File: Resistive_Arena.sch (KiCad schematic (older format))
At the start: 15 parts, among them P1 1360_2_PIN, P2 1360_2_PIN, P3 1360_2_PIN, P4 1360_2_PIN, P5 1360_2_PIN, P6 1360_2_PIN, P7 1360_2_PIN, P8 1360_2_PIN

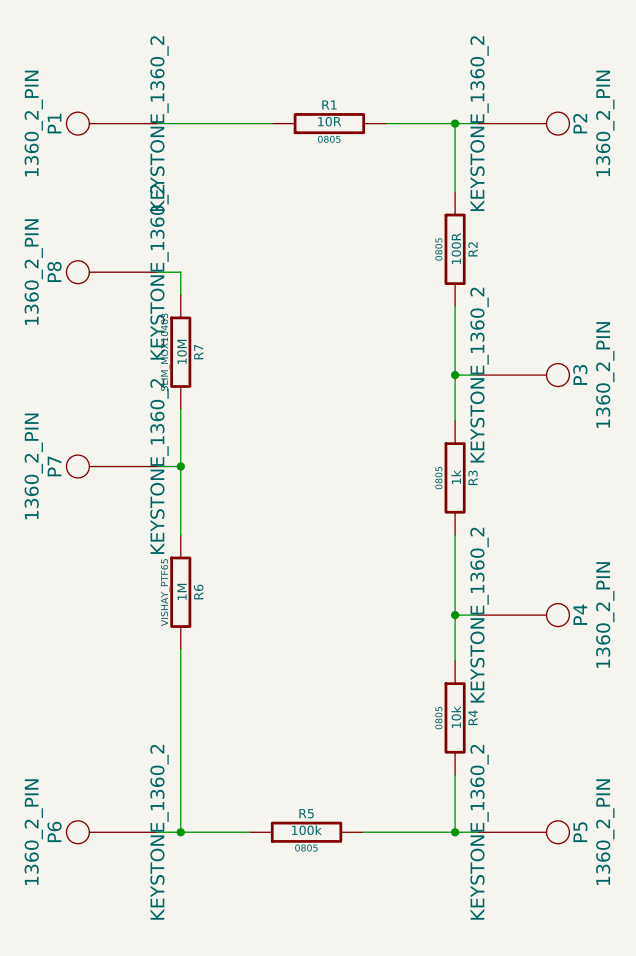
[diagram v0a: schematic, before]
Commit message: Added models for 3D pcb view
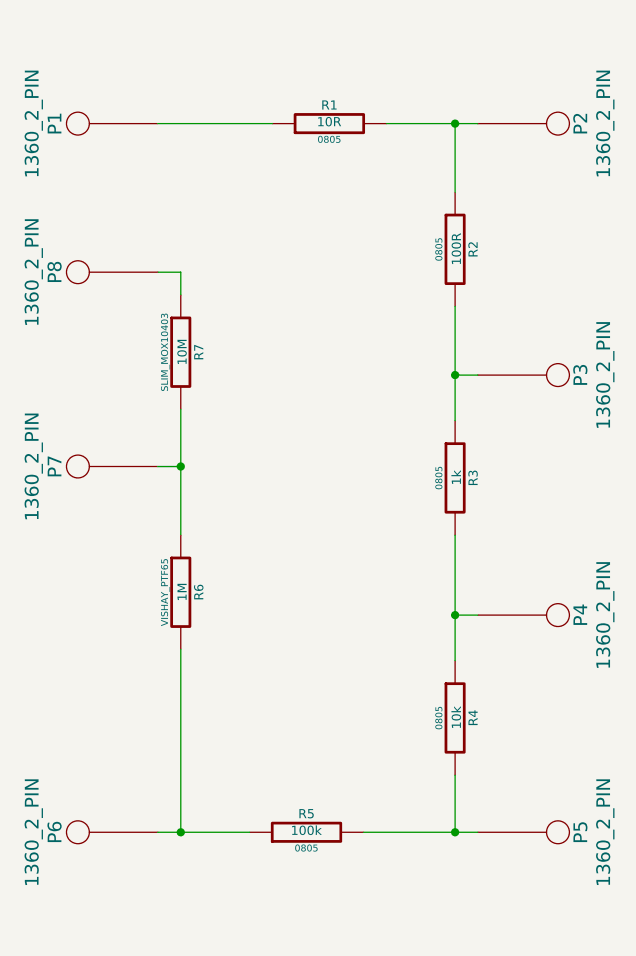
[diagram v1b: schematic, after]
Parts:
- P1, P2, P3, P4, P5, P6, P7, P8: Manufacturer (none) -> Keystone; Part Number (none) -> 1360-2; Source (none) -> Mouser
- R1: Manufacturer (none) -> TE Connectivity; Part Number (none) -> RN73C2A10RBTG; Source (none) -> Mouser
- R2: Manufacturer (none) -> Welwyn-TT; Part Number (none) -> PCF0805-13-100RBT1; Source (none) -> Mouser
- R3: Manufacturer (none) -> Welwyn-TT; Part Number (none) -> PCF0805-13-1K0BT1; Source (none) -> Mouser
- R4: Manufacturer (none) -> Welwyn-TT; Part Number (none) -> PCF0805-13-10KBT1; Source (none) -> Mouser
- R5: Manufacturer (none) -> Vishay; Part Number (none) -> TNPU0805100KAZEN00; Source (none) -> Mouser
- R6: Manufacturer (none) -> Vishay; Part Number (none) -> PTF651M0000BZBF; Source (none) -> Mouser
- R7: Manufacturer (none) -> Ohmite; Part Number (none) -> SM104031005FE; Source (none) -> Mouser
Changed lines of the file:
@@
 F 1 "10R" V 5157 1701 40  0000 C CNN
 F 2 "0805" V 5080 1700 30  0000 C CNN
-F 3 "" H 5150 1700 30  0000 C CNN
+F 3 "http://documents.tycoelectronics.com/commerce/DocumentDelivery/DDEController?Action=showdoc&DocId=Data+Sheet%7F1773270%7FK%7Fpdf%7FEnglish%7FENG_DS_1773270_K.pdf" H 5150 1700 30  0001 C CNN
+F 4 "TE Connectivity" V 5150 1700 60  0001 C CNN "Manufacturer"
+F 5 "RN73C2A10RBTG" V 5150 1700 60  0001 C CNN "Part Number"
+F 6 "Mouser" V 5150 1700 60  0001 C CNN "Source"
 	1    5150 1700
 	0    -1   -1   0
@@
 F 1 "100R" V 5707 2251 40  0000 C CNN
 F 2 "0805" V 5630 2250 30  0000 C CNN
-F 3 "" H 5700 2250 30  0000 C CNN
+F 3 "http://www.welwyn-tt.com/pdf/datasheet/PCF.pdf" H 5700 2250 30  0001 C CNN
+F 4 "Welwyn-TT" V 5700 2250 60  0001 C CNN "Manufacturer"
+F 5 "PCF0805-13-100RBT1" V 5700 2250 60  0001 C CNN "Part Number"
+F 6 "Mouser" V 5700 2250 60  0001 C CNN "Source"
 	1    5700 2250
 	1    0    0    -1
@@
 F 1 "1k" V 5707 3251 40  0000 C CNN
 F 2 "0805" V 5630 3250 30  0000 C CNN
-F 3 "" H 5700 3250 30  0000 C CNN
+F 3 "http://www.welwyn-tt.com/pdf/datasheet/PCF.pdf" H 5700 3250 30  0001 C CNN
+F 4 "Welwyn-TT" V 5700 3250 60  0001 C CNN "Manufacturer"
+F 5 "PCF0805-13-1K0BT1" V 5700 3250 60  0001 C CNN "Part Number"
+F 6 "Mouser" V 5700 3250 60  0001 C CNN "Source"
 	1    5700 3250
 	1    0    0    -1
@@
 F 1 "10k" V 5707 4301 40  0000 C CNN
 F 2 "0805" V 5630 4300 30  0000 C CNN
-F 3 "" H 5700 4300 30  0000 C CNN
+F 3 "http://www.welwyn-tt.com/pdf/datasheet/PCF.pdf" H 5700 4300 30  0001 C CNN
+F 4 "Welwyn-TT" V 5700 4300 60  0001 C CNN "Manufacturer"
+F 5 "PCF0805-13-10KBT1" V 5700 4300 60  0001 C CNN "Part Number"
+F 6 "Mouser" V 5700 4300 60  0001 C CNN "Source"
 	1    5700 4300
 	1    0    0    -1
@@
 F 1 "100k" V 5057 4801 40  0000 C CNN
 F 2 "0805" V 4980 4800 30  0000 C CNN
-F 3 "" H 5050 4800 30  0000 C CNN
+F 3 "http://www.vishay.com/docs/28779/tnpu_e3.pdf" H 5050 4800 30  0001 C CNN
+F 4 "Vishay" V 5050 4800 60  0001 C CNN "Manufacturer"
+F 5 "TNPU0805100KAZEN00" V 5050 4800 60  0001 C CNN "Part Number"
+F 6 "Mouser" V 5050 4800 60  0001 C CNN "Source"
 	1    5050 4800
 	0    -1   -1   0
@@
 F 1 "1M" V 4507 3751 40  0000 C CNN
 F 2 "VISHAY_PTF65" V 4430 3750 30  0000 C CNN
-F 3 "" H 4500 3750 30  0000 C CNN
+F 3 "http://www.vishay.com/docs/31019/ptf.pdf" H 4500 3750 30  0001 C CNN
+F 4 "Vishay" V 4500 3750 60  0001 C CNN "Manufacturer"
+F 5 "PTF651M0000BZBF" V 4500 3750 60  0001 C CNN "Part Number"
+F 6 "Mouser" V 4500 3750 60  0001 C CNN "Source"
 	1    4500 3750
 	1    0    0    -1
@@
 F 1 "10M" V 4507 2701 40  0000 C CNN
 F 2 "SLIM_MOX10403" V 4430 2700 30  0000 C CNN
-F 3 "" H 4500 2700 30  0000 C CNN
+F 3 "http://www.ohmite.com/catalog/pdf/v_slimmox.pdf" H 4500 2700 30  0001 C CNN
+F 4 "Ohmite" V 4500 2700 60  0001 C CNN "Manufacturer"
+F 5 "SM104031005FE" V 4500 2700 60  0001 C CNN "Part Number"
+F 6 "Mouser" V 4500 2700 60  0001 C CNN "Source"
 	1    4500 2700
 	1    0    0    -1
@@
 Wire Wire Line
 	4400 1700 4900 1700
-$Comp
-L 1360_2_PIN P2
-U 1 1 537D084F
-P 5800 1700
-F 0 "P2" H 5800 2150 60  0000 C CNN
-F 1 "1360_2_PIN" H 5800 2250 60  0000 C CNN
-F 2 "KEYSTONE_1360_2" H 5800 1700 60  0000 C CNN
-F 3 "" H 5800 1700 60  0000 C CNN
-	1    5800 1700
-	0    1    1    0
-$EndComp
-$Comp
-L 1360_2_PIN P3
-U 1 1 537D0863
-P 5800 2800
-F 0 "P3" H 5800 3250 60  0000 C CNN
-F 1 "1360_2_PIN" H 5800 3350 60  0000 C CNN
-F 2 "KEYSTONE_1360_2" H 5800 2800 60  0000 C CNN
-F 3 "" H 5800 2800 60  0000 C CNN
-	1    5800 2800
-	0    1    1    0
-$EndComp
-$Comp
-L 1360_2_PIN P4
-U 1 1 537D0877
-P 5800 3850
-F 0 "P4" H 5800 4300 60  0000 C CNN
-F 1 "1360_2_PIN" H 5800 4400 60  0000 C CNN
-F 2 "KEYSTONE_1360_2" H 5800 3850 60  0000 C CNN
-F 3 "" H 5800 3850 60  0000 C CNN
-	1    5800 3850
-	0    1    1    0
-$EndComp
-$Comp
-L 1360_2_PIN P5
-U 1 1 537D088B
-P 5800 4800
-F 0 "P5" H 5800 5250 60  0000 C CNN
-F 1 "1360_2_PIN" H 5800 5350 60  0000 C CNN
-F 2 "KEYSTONE_1360_2" H 5800 4800 60  0000 C CNN
-F 3 "" H 5800 4800 60  0000 C CNN
-	1    5800 4800
-	0    1    1    0
-$EndComp
-$Comp
-L 1360_2_PIN P6
-U 1 1 537D089F
-P 4400 4800
-F 0 "P6" H 4400 5250 60  0000 C CNN
-F 1 "1360_2_PIN" H 4400 5350 60  0000 C CNN
-F 2 "KEYSTONE_1360_2" H 4400 4800 60  0000 C CNN
-F 3 "" H 4400 4800 60  0000 C CNN
-	1    4400 4800
-	0    -1   -1   0
-$EndComp
-$Comp
-L 1360_2_PIN P7
-U 1 1 537D08B3
-P 4400 3200
-F 0 "P7" H 4400 3650 60  0000 C CNN
-F 1 "1360_2_PIN" H 4400 3750 60  0000 C CNN
-F 2 "KEYSTONE_1360_2" H 4400 3200 60  0000 C CNN
-F 3 "" H 4400 3200 60  0000 C CNN
-	1    4400 3200
-	0    -1   -1   0
-$EndComp
-$Comp
-L 1360_2_PIN P1
-U 1 1 537D08C7
-P 4400 1700
-F 0 "P1" H 4400 2150 60  0000 C CNN
-F 1 "1360_2_PIN" H 4400 2250 60  0000 C CNN
-F 2 "KEYSTONE_1360_2" H 4400 1700 60  0000 C CNN
-F 3 "" H 4400 1700 60  0000 C CNN
-	1    4400 1700
-	0    -1   -1   0
-$EndComp
 Connection ~ 5700 1700
 Wire Wire Line
@@
 	4400 3200 4500 3200
 Connection ~ 4500 3200
+Wire Wire Line
+	4500 2450 4500 2350
+Wire Wire Line
+	4500 2350 4400 2350
+$Comp
+L 1360_2_PIN P1
+U 1 1 5390DAA8
+P 4400 1700
+F 0 "P1" H 4400 2150 60  0000 C CNN
+F 1 "1360_2_PIN" H 4400 2250 60  0000 C CNN
+F 2 "KEYSTONE_1360_2" H 4300 2050 60  0001 C CNN
+F 3 "http://www.keyelco.com/product.cfm/product_id/3057" H 4400 2150 60  0001 C CNN
+F 4 "Keystone" H 4500 2250 60  0001 C CNN "Manufacturer"
+F 5 "1360-2" H 4600 2350 60  0001 C CNN "Part Number"
+F 6 "Mouser" H 4700 2450 60  0001 C CNN "Source"
+	1    4400 1700
+	0    -1   -1   0
+$EndComp
+$Comp
+L 1360_2_PIN P2
+U 1 1 5390DACD
+P 5800 1700
+F 0 "P2" H 5800 2150 60  0000 C CNN
+F 1 "1360_2_PIN" H 5800 2250 60  0000 C CNN
+F 2 "KEYSTONE_1360_2" H 5700 2050 60  0001 C CNN
+F 3 "http://www.keyelco.com/product.cfm/product_id/3057" H 5800 2150 60  0001 C CNN
+F 4 "Keystone" H 5900 2250 60  0001 C CNN "Manufacturer"
+F 5 "1360-2" H 6000 2350 60  0001 C CNN "Part Number"
+F 6 "Mouser" H 6100 2450 60  0001 C CNN "Source"
+	1    5800 1700
+	0    1    1    0
+$EndComp
+$Comp
+L 1360_2_PIN P3
+U 1 1 5390DAF2
+P 5800 2800
+F 0 "P3" H 5800 3250 60  0000 C CNN
+F 1 "1360_2_PIN" H 5800 3350 60  0000 C CNN
+F 2 "KEYSTONE_1360_2" H 5700 3150 60  0001 C CNN
+F 3 "http://www.keyelco.com/product.cfm/product_id/3057" H 5800 3250 60  0001 C CNN
+F 4 "Keystone" H 5900 3350 60  0001 C CNN "Manufacturer"
+F 5 "1360-2" H 6000 3450 60  0001 C CNN "Part Number"
+F 6 "Mouser" H 6100 3550 60  0001 C CNN "Source"
+	1    5800 2800
+	0    1    1    0
+$EndComp
+$Comp
+L 1360_2_PIN P4
+U 1 1 5390DB17
+P 5800 3850
+F 0 "P4" H 5800 4300 60  0000 C CNN
+F 1 "1360_2_PIN" H 5800 4400 60  0000 C CNN
+F 2 "KEYSTONE_1360_2" H 5700 4200 60  0001 C CNN
+F 3 "http://www.keyelco.com/product.cfm/product_id/3057" H 5800 4300 60  0001 C CNN
+F 4 "Keystone" H 5900 4400 60  0001 C CNN "Manufacturer"
+F 5 "1360-2" H 6000 4500 60  0001 C CNN "Part Number"
+F 6 "Mouser" H 6100 4600 60  0001 C CNN "Source"
+	1    5800 3850
+	0    1    1    0
+$EndComp
+$Comp
+L 1360_2_PIN P5
+U 1 1 5390DB3C
+P 5800 4800
+F 0 "P5" H 5800 5250 60  0000 C CNN
+F 1 "1360_2_PIN" H 5800 5350 60  0000 C CNN
+F 2 "KEYSTONE_1360_2" H 5700 5150 60  0001 C CNN
+F 3 "http://www.keyelco.com/product.cfm/product_id/3057" H 5800 5250 60  0001 C CNN
+F 4 "Keystone" H 5900 5350 60  0001 C CNN "Manufacturer"
+F 5 "1360-2" H 6000 5450 60  0001 C CNN "Part Number"
+F 6 "Mouser" H 6100 5550 60  0001 C CNN "Source"
+	1    5800 4800
+	0    1    1    0
+$EndComp
+$Comp
+L 1360_2_PIN P6
+U 1 1 5390DB61
+P 4400 4800
+F 0 "P6" H 4400 5250 60  0000 C CNN
+F 1 "1360_2_PIN" H 4400 5350 60  0000 C CNN
+F 2 "KEYSTONE_1360_2" H 4300 5150 60  0001 C CNN
+F 3 "http://www.keyelco.com/product.cfm/product_id/3057" H 4400 5250 60  0001 C CNN
+F 4 "Keystone" H 4500 5350 60  0001 C CNN "Manufacturer"
+F 5 "1360-2" H 4600 5450 60  0001 C CNN "Part Number"
+F 6 "Mouser" H 4700 5550 60  0001 C CNN "Source"
+	1    4400 4800
+	0    -1   -1   0
+$EndComp
+$Comp
+L 1360_2_PIN P7
+U 1 1 5390DB86
+P 4400 3200
+F 0 "P7" H 4400 3650 60  0000 C CNN
+F 1 "1360_2_PIN" H 4400 3750 60  0000 C CNN
+F 2 "KEYSTONE_1360_2" H 4300 3550 60  0001 C CNN
+F 3 "http://www.keyelco.com/product.cfm/product_id/3057" H 4400 3650 60  0001 C CNN
+F 4 "Keystone" H 4500 3750 60  0001 C CNN "Manufacturer"
+F 5 "1360-2" H 4600 3850 60  0001 C CNN "Part Number"
+F 6 "Mouser" H 4700 3950 60  0001 C CNN "Source"
+	1    4400 3200
+	0    -1   -1   0
+$EndComp
 $Comp
 L 1360_2_PIN P8
-U 1 1 537E641A
+U 1 1 5390DBAB
 P 4400 2350
 F 0 "P8" H 4400 2800 60  0000 C CNN
 F 1 "1360_2_PIN" H 4400 2900 60  0000 C CNN
-F 2 "KEYSTONE_1360_2" H 4400 2350 60  0000 C CNN
-F 3 "" H 4400 2350 60  0000 C CNN
+F 2 "KEYSTONE_1360_2" H 4300 2700 60  0001 C CNN
+F 3 "http://www.keyelco.com/product.cfm/product_id/3057" H 4400 2800 60  0001 C CNN
+F 4 "Keystone" H 4500 2900 60  0001 C CNN "Manufacturer"
+F 5 "1360-2" H 4600 3000 60  0001 C CNN "Part Number"
+F 6 "Mouser" H 4700 3100 60  0001 C CNN "Source"
 	1    4400 2350
 	0    -1   -1   0
 $EndComp
-Wire Wire Line
-	4500 2450 4500 2350
-Wire Wire Line
-	4500 2350 4400 2350
 $EndSCHEMATC
